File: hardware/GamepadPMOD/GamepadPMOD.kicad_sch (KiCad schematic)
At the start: 23 parts, among them J3 10129382-912001BLF, J4 613012243121, J5 Conn_02x03_Odd_Even, SW1 434121025816, U1 CH32V003F4U6

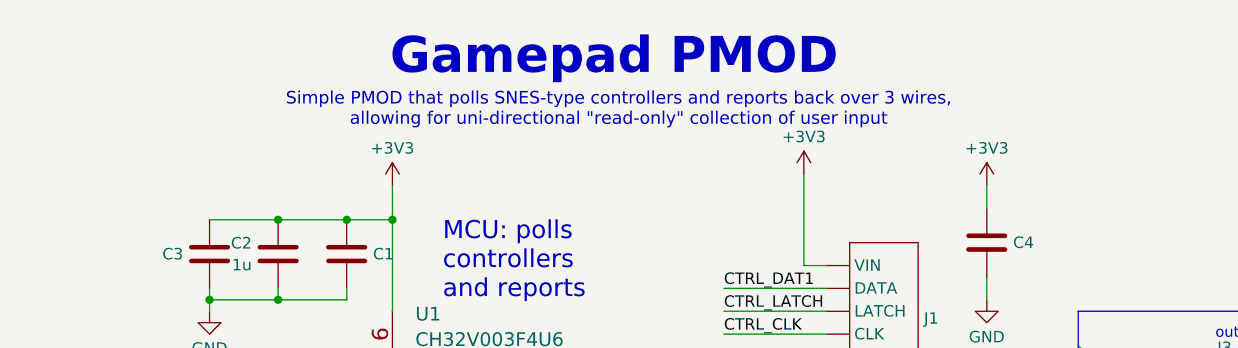
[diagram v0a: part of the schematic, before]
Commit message: PCB v1.3: TT designed for logo, slightly larger drill for SFC conn
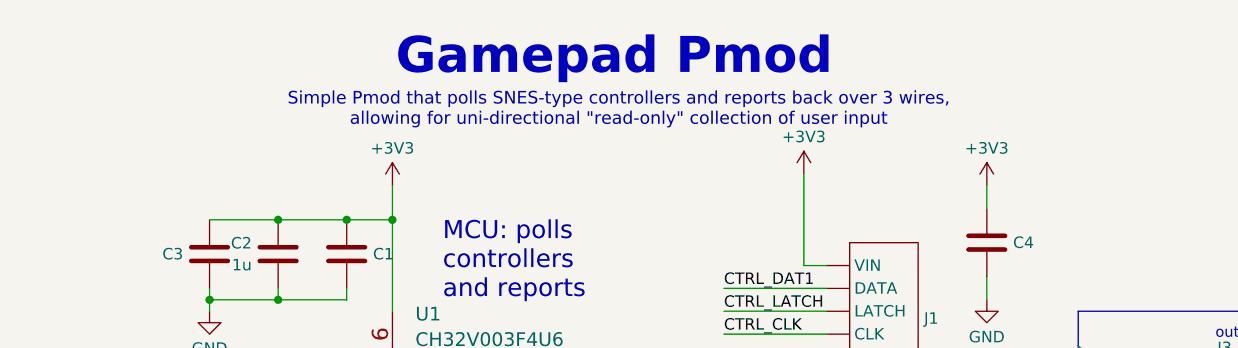
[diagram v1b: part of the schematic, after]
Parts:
- C1, C4, C5, C6: Characteristics (none) -> 0805 10uF; LCSC (none) -> C1713; MPN GRM21BR6YA106KE43L -> CL21A106KOQNNNE
- C2, C7: Characteristics (none) -> 0603 1uF; LCSC (none) -> C15849; MPN GRT188R61H105KE13D -> CL10A105KB8NNNC
- C3, C8: Characteristics (none) -> 0402 100nF; LCSC (none) -> C1525; MPN GRM155R71H104KE14J -> CL05B104KO5NNNC
- D1: Characteristics (none) -> LED orange; LCSC (none) -> C965800
- J1: value ~ -> SFC connector R/A; Characteristics (none) -> SFC/SNES controller connector
- J2: value ~ -> SFC connector VERT; Characteristics (none) -> SFC/SNES controller connector
- J3: Characteristics (none) -> 2x6 100mil male R/A; LCSC (none) -> C492434
- J4: Characteristics (none) -> 2x6 100mil female; LCSC (none) -> C541855
- J5: Characteristics (none) -> 2x3 100mil; LCSC (none) -> C492420
- R1: LCSC (none) -> C60490; MPN ERJ-U02F1002X -> RC0402FR-0710KL
- R2: Characteristics (none) -> 0402 1k; LCSC (none) -> C106235; MPN CRG0402F1K0 -> RC0402FR-071KL
- R3: value R_1k_0402 -> 200R; Characteristics (none) -> 0402 200R; DigikeyPN A121534CT-ND -> (none); Display Value 1k -> 200R; LCSC (none) -> C114764; MPN CRG0402F1K0 -> RC0402FR-07200RL
- SW1: LCSC (none) -> C4364640
- U1: Characteristics (none) -> CH32V003 MCU; LCSC (none) -> C5299908; MPN (none) -> CH32V003F4U6
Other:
- note added: "Gamepad Pmod"
- note added: "Simple Pmod that polls SNES-type controllers and reports back over 3 wires, allowing for uni-directional "read-only" collection of user input"
- note removed: "Gamepad PMOD"
- note removed: "Simple PMOD that polls SNES-type controllers and reports back over 3 wires, allowing for uni-directional "read-only" collection of user input"

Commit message: Modified pmod, breaking 1U width to allow for 2 vertical SFC connectors
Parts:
- J1: value SFC connector R/A -> SFC connector VERT
